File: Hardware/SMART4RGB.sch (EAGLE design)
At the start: 14 parts, among them IC1 WS2811-SOP8, IC2 WS2811-SOP8, IC3 WS2811-SOP8, IC4 WS2811-SOP8, SW1 QG16F-RGB, SW2 QG16F-RGB, SW3 QG16F-RGB, SW4 QG16F-RGB

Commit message: Alter size of board and hole locations to match updated controller. Switch green and blue connections to make colours match WS2812 profile.
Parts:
- C1, C2, C3, C4: device freetronics-jon:CAP0603 -> SuperHouse-DiscreteSemi:CAP0603
- H1: value M06X22MM -> M02X6-SOCKET; device freetronics-jon:M06X22MM -> SuperHouse-Connectors:M02X6-SOCKET
- IC1, IC2, IC3, IC4: device freetronics-jon:WS2811-SOP8 -> SuperHouse-ICs:WS2811-SOP8
- R1: device freetronics-jon:RESISTOR0603 -> SuperHouse-DiscreteSemi:RESISTOR0603
- SW1, SW2, SW3, SW4: device freetronics-jon:QG16F-RGB -> SuperHouse-Switches:QG16F-RGB
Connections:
- net LED1B: now also SW1.G; no longer SW1.B
- net LED1G: now also SW1.B; no longer SW1.G
- net LED2B: now also SW2.G; no longer SW2.B
- net LED2G: now also SW2.B; no longer SW2.G
- net LED3B: now also SW3.G; no longer SW3.B
- net LED3G: now also SW3.B; no longer SW3.G
- net LED4B: now also SW4.G; no longer SW4.B
- net LED4G: now also SW4.B; no longer SW4.G
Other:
- note added: "(C)2018-2020 SuperHouse Automation Pty Ltd: www.superhouse.tv"
- note added: "Green / blue outputs are reversed on WS2811 when controlled using the WS2812 drivers. LED lines switched to make the output match colour commands."
- note added: "V2.0 (2020-11-06)"
- note removed: "(C)2018 SuperHouse Automation Pty Ltd: www.superhouse.tv"
- note removed: "V1.0 (2018-04-11)"

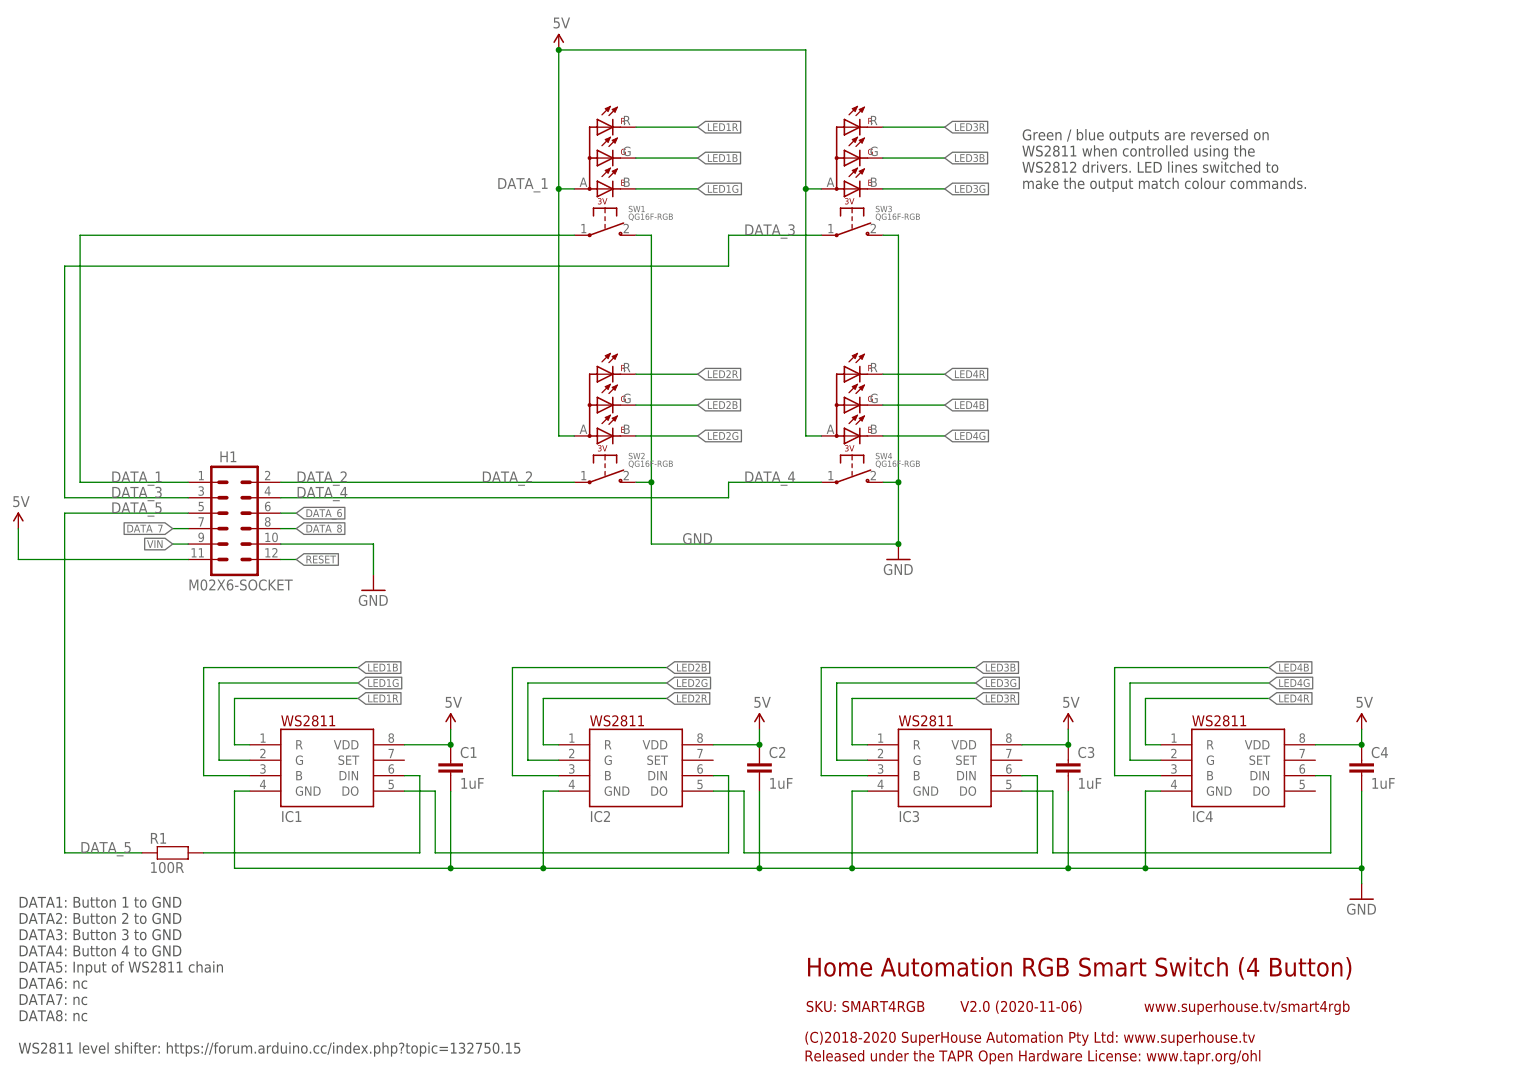
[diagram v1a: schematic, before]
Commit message: Converted switch isolation from FETs to diodes for v2.1 release.
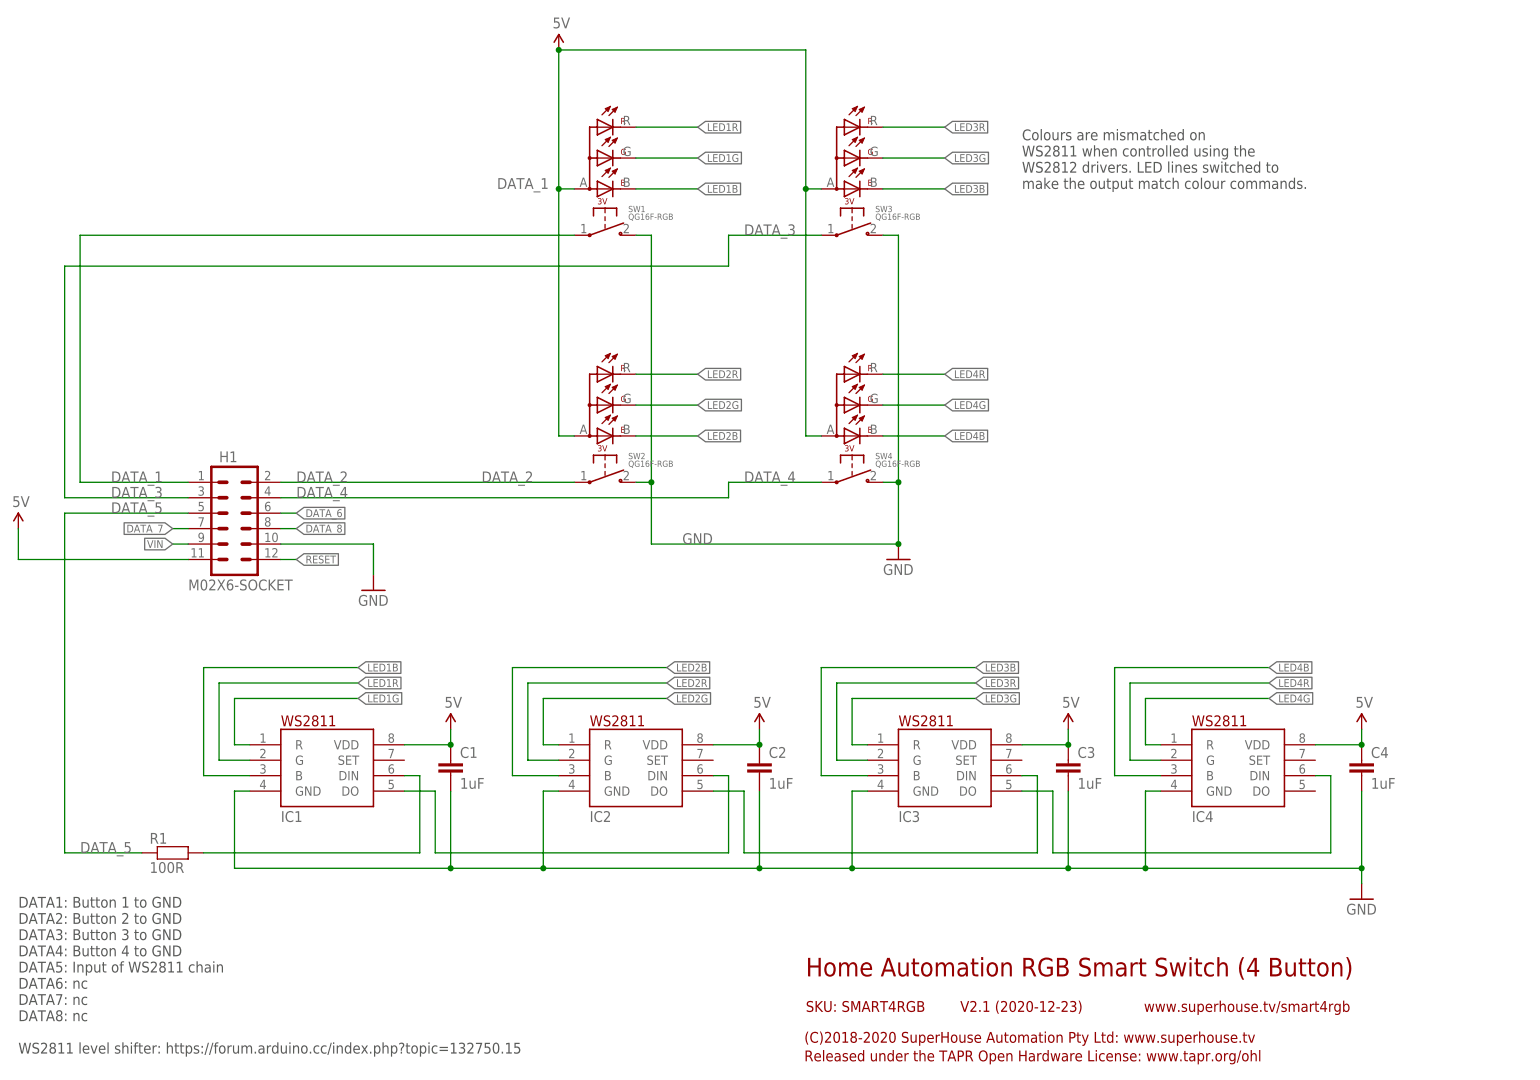
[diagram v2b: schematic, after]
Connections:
- net LED1B: now also SW1.B; no longer SW1.G
- net LED1G: now also IC1.R, SW1.G; no longer IC1.G, SW1.B
- net LED1R: now also IC1.G; no longer IC1.R
- net LED2B: now also SW2.B; no longer SW2.G
- net LED2G: now also IC2.R, SW2.G; no longer IC2.G, SW2.B
- net LED2R: now also IC2.G; no longer IC2.R
- net LED3B: now also SW3.B; no longer SW3.G
- net LED3G: now also IC3.R, SW3.G; no longer IC3.G, SW3.B
- net LED3R: now also IC3.G; no longer IC3.R
- net LED4B: now also SW4.B; no longer SW4.G
- net LED4G: now also IC4.R, SW4.G; no longer IC4.G, SW4.B
- net LED4R: now also IC4.G; no longer IC4.R
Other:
- note added: "Colours are mismatched on WS2811 when controlled using the WS2812 drivers. LED lines switched to make the output match colour commands."
- note added: "V2.1 (2020-12-23)"
- note removed: "Green / blue outputs are reversed on WS2811 when controlled using the WS2812 drivers. LED lines switched to make the output match colour commands."
- note removed: "V2.0 (2020-11-06)"
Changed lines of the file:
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@@
 <frame x1="0" y1="0" x2="248.92" y2="185.42" columns="8" rows="5" layer="94"/>
 <text x="139.7" y="20.32" size="3.048" layer="94">Home Automation RGB Smart Switch (4 Button)</text>
-<text x="165.1" y="14.478" size="1.778" layer="94">V2.0 (2020-11-06)</text>
+<text x="165.1" y="14.478" size="1.778" layer="94">V2.1 (2020-12-23)</text>
 <text x="139.7" y="14.478" size="1.778" layer="94">SKU: SMART4RGB</text>
 <text x="139.446" y="9.398" size="1.778" layer="94">(C)2018-2020 SuperHouse Automation Pty Ltd: www.superhouse.tv</text>
@@
 DATA8: nc
 WS2811 level shifter: https://forum.arduino.cc/index.php?topic=132750.15</text>
-<text x="175.26" y="149.86" size="1.778" layer="97">Green / blue outputs are reversed on
+<text x="175.26" y="149.86" size="1.778" layer="97">Colours are mismatched on
 WS2811 when controlled using the
 WS2812 drivers. LED lines switched to
@@
 </segment>
 <segment>
-<pinref part="SW1" gate="G$1" pin="G"/>
-<wire x1="111.76" y1="154.94" x2="121.92" y2="154.94" width="0.1524" layer="91"/>
-<label x="121.92" y="154.94" size="1.27" layer="95" xref="yes"/>
+<wire x1="111.76" y1="149.86" x2="121.92" y2="149.86" width="0.1524" layer="91"/>
+<pinref part="SW1" gate="G$1" pin="B"/>
+<label x="121.92" y="149.86" size="1.27" layer="95" xref="yes"/>
 </segment>
 </net>
@@
 </segment>
 <segment>
-<pinref part="SW2" gate="G$1" pin="G"/>
-<wire x1="111.76" y1="114.3" x2="121.92" y2="114.3" width="0.1524" layer="91"/>
-<label x="121.92" y="114.3" size="1.27" layer="95" xref="yes"/>
+<wire x1="111.76" y1="109.22" x2="121.92" y2="109.22" width="0.1524" layer="91"/>
+<pinref part="SW2" gate="G$1" pin="B"/>
+<label x="121.92" y="109.22" size="1.27" layer="95" xref="yes"/>
 </segment>
 </net>
@@
 </segment>
 <segment>
-<pinref part="SW3" gate="G$1" pin="G"/>
-<wire x1="152.4" y1="154.94" x2="162.56" y2="154.94" width="0.1524" layer="91"/>
-<label x="162.56" y="154.94" size="1.27" layer="95" xref="yes"/>
+<wire x1="152.4" y1="149.86" x2="162.56" y2="149.86" width="0.1524" layer="91"/>
+<pinref part="SW3" gate="G$1" pin="B"/>
+<label x="162.56" y="149.86" size="1.27" layer="95" xref="yes"/>
 </segment>
 </net>
@@
 </segment>
 <segment>
-<pinref part="SW4" gate="G$1" pin="G"/>
-<wire x1="152.4" y1="114.3" x2="162.56" y2="114.3" width="0.1524" layer="91"/>
-<label x="162.56" y="114.3" size="1.27" layer="95" xref="yes"/>
+<wire x1="152.4" y1="109.22" x2="162.56" y2="109.22" width="0.1524" layer="91"/>
+<pinref part="SW4" gate="G$1" pin="B"/>
+<label x="162.56" y="109.22" size="1.27" layer="95" xref="yes"/>
 </segment>
 </net>
@@
 </segment>
 <segment>
+<pinref part="IC1" gate="G$1" pin="G"/>
+<wire x1="48.26" y1="55.88" x2="43.18" y2="55.88" width="0.1524" layer="91"/>
+<wire x1="43.18" y1="55.88" x2="43.18" y2="68.58" width="0.1524" layer="91"/>
+<wire x1="43.18" y1="68.58" x2="66.04" y2="68.58" width="0.1524" layer="91"/>
+<label x="66.04" y="68.58" size="1.27" layer="95" xref="yes"/>
+</segment>
+</net>
+<net name="LED1G" class="0">
+<segment>
+<pinref part="SW1" gate="G$1" pin="G"/>
+<wire x1="111.76" y1="154.94" x2="121.92" y2="154.94" width="0.1524" layer="91"/>
+<label x="121.92" y="154.94" size="1.27" layer="95" xref="yes"/>
+</segment>
+<segment>
 <pinref part="IC1" gate="G$1" pin="R"/>
 <wire x1="48.26" y1="58.42" x2="45.72" y2="58.42" width="0.1524" layer="91"/>
@@
 </segment>
 </net>
-<net name="LED1G" class="0">
-<segment>
-<pinref part="IC1" gate="G$1" pin="G"/>
-<wire x1="48.26" y1="55.88" x2="43.18" y2="55.88" width="0.1524" layer="91"/>
-<wire x1="43.18" y1="55.88" x2="43.18" y2="68.58" width="0.1524" layer="91"/>
-<wire x1="43.18" y1="68.58" x2="66.04" y2="68.58" width="0.1524" layer="91"/>
-<label x="66.04" y="68.58" size="1.27" layer="95" xref="yes"/>
-</segment>
-<segment>
-<wire x1="111.76" y1="149.86" x2="121.92" y2="149.86" width="0.1524" layer="91"/>
-<pinref part="SW1" gate="G$1" pin="B"/>
-<label x="121.92" y="149.86" size="1.27" layer="95" xref="yes"/>
-</segment>
-</net>
 <net name="LED3G" class="0">
+<segment>
+<pinref part="SW3" gate="G$1" pin="G"/>
+<wire x1="152.4" y1="154.94" x2="162.56" y2="154.94" width="0.1524" layer="91"/>
+<label x="162.56" y="154.94" size="1.27" layer="95" xref="yes"/>
+</segment>
+<segment>
+<pinref part="IC3" gate="G$1" pin="R"/>
+<wire x1="149.86" y1="58.42" x2="147.32" y2="58.42" width="0.1524" layer="91"/>
+<wire x1="147.32" y1="58.42" x2="147.32" y2="66.04" width="0.1524" layer="91"/>
+<wire x1="147.32" y1="66.04" x2="167.64" y2="66.04" width="0.1524" layer="91"/>
+<label x="167.64" y="66.04" size="1.27" layer="95" xref="yes"/>
+</segment>
+</net>
+<net name="LED3R" class="0">
+<segment>
+<pinref part="SW3" gate="G$1" pin="R"/>
+<wire x1="152.4" y1="160.02" x2="162.56" y2="160.02" width="0.1524" layer="91"/>
+<label x="162.56" y="160.02" size="1.27" layer="95" xref="yes"/>
+</segment>
 <segment>
 <pinref part="IC3" gate="G$1" pin="G"/>
@@
 <label x="167.64" y="68.58" size="1.27" layer="95" xref="yes"/>
 </segment>
-<segment>
-<wire x1="152.4" y1="149.86" x2="162.56" y2="149.86" width="0.1524" layer="91"/>
-<pinref part="SW3" gate="G$1" pin="B"/>
-<label x="162.56" y="149.86" size="1.27" layer="95" xref="yes"/>
-</segment>
-</net>
-<net name="LED3R" class="0">
-<segment>
-<pinref part="SW3" gate="G$1" pin="R"/>
-<wire x1="152.4" y1="160.02" x2="162.56" y2="160.02" width="0.1524" layer="91"/>
-<label x="162.56" y="160.02" size="1.27" layer="95" xref="yes"/>
-</segment>
-<segment>
-<pinref part="IC3" gate="G$1" pin="R"/>
-<wire x1="149.86" y1="58.42" x2="147.32" y2="58.42" width="0.1524" layer="91"/>
-<wire x1="147.32" y1="58.42" x2="147.32" y2="66.04" width="0.1524" layer="91"/>
-<wire x1="147.32" y1="66.04" x2="167.64" y2="66.04" width="0.1524" layer="91"/>
-<label x="167.64" y="66.04" size="1.27" layer="95" xref="yes"/>
-</segment>
 </net>
 <net name="LED2G" class="0">
+<segment>
+<pinref part="SW2" gate="G$1" pin="G"/>
+<wire x1="111.76" y1="114.3" x2="121.92" y2="114.3" width="0.1524" layer="91"/>
+<label x="121.92" y="114.3" size="1.27" layer="95" xref="yes"/>
+</segment>
+<segment>
+<pinref part="IC2" gate="G$1" pin="R"/>
+<wire x1="99.06" y1="58.42" x2="96.52" y2="58.42" width="0.1524" layer="91"/>
+<wire x1="96.52" y1="58.42" x2="96.52" y2="66.04" width="0.1524" layer="91"/>
+<wire x1="96.52" y1="66.04" x2="116.84" y2="66.04" width="0.1524" layer="91"/>
+<label x="116.84" y="66.04" size="1.27" layer="95" xref="yes"/>
+</segment>
+</net>
+<net name="LED2R" class="0">
+<segment>
+<pinref part="SW2" gate="G$1" pin="R"/>
+<wire x1="111.76" y1="119.38" x2="121.92" y2="119.38" width="0.1524" layer="91"/>
+<label x="121.92" y="119.38" size="1.27" layer="95" xref="yes"/>
+</segment>
 <segment>
 <pinref part="IC2" gate="G$1" pin="G"/>
@@
 <label x="116.84" y="68.58" size="1.27" layer="95" xref="yes"/>
 </segment>
-<segment>
-<wire x1="111.76" y1="109.22" x2="121.92" y2="109.22" width="0.1524" layer="91"/>
-<pinref part="SW2" gate="G$1" pin="B"/>
-<label x="121.92" y="109.22" size="1.27" layer="95" xref="yes"/>
-</segment>
-</net>
-<net name="LED2R" class="0">
-<segment>
-<pinref part="SW2" gate="G$1" pin="R"/>
-<wire x1="111.76" y1="119.38" x2="121.92" y2="119.38" width="0.1524" layer="91"/>
-<label x="121.92" y="119.38" size="1.27" layer="95" xref="yes"/>
-</segment>
-<segment>
-<pinref part="IC2" gate="G$1" pin="R"/>
-<wire x1="99.06" y1="58.42" x2="96.52" y2="58.42" width="0.1524" layer="91"/>
-<wire x1="96.52" y1="58.42" x2="96.52" y2="66.04" width="0.1524" layer="91"/>
-<wire x1="96.52" y1="66.04" x2="116.84" y2="66.04" width="0.1524" layer="91"/>
-<label x="116.84" y="66.04" size="1.27" layer="95" xref="yes"/>
-</segment>
 </net>
 <net name="LED4G" class="0">
+<segment>
+<pinref part="SW4" gate="G$1" pin="G"/>
+<wire x1="152.4" y1="114.3" x2="162.56" y2="114.3" width="0.1524" layer="91"/>
+<label x="162.56" y="114.3" size="1.27" layer="95" xref="yes"/>
+</segment>
+<segment>
+<pinref part="IC4" gate="G$1" pin="R"/>
+<wire x1="198.12" y1="58.42" x2="195.58" y2="58.42" width="0.1524" layer="91"/>
+<wire x1="195.58" y1="58.42" x2="195.58" y2="66.04" width="0.1524" layer="91"/>
+<wire x1="195.58" y1="66.04" x2="215.9" y2="66.04" width="0.1524" layer="91"/>
+<label x="215.9" y="66.04" size="1.27" layer="95" xref="yes"/>
+</segment>
+</net>
+<net name="LED4R" class="0">
+<segment>
+<pinref part="SW4" gate="G$1" pin="R"/>
+<wire x1="152.4" y1="119.38" x2="162.56" y2="119.38" width="0.1524" layer="91"/>
+<label x="162.56" y="119.38" size="1.27" layer="95" xref="yes"/>
+</segment>
 <segment>
 <pinref part="IC4" gate="G$1" pin="G"/>
@@
 <label x="215.9" y="68.58" size="1.27" layer="95" xref="yes"/>
 </segment>
-<segment>
-<wire x1="152.4" y1="109.22" x2="162.56" y2="109.22" width="0.1524" layer="91"/>
-<pinref part="SW4" gate="G$1" pin="B"/>
-<label x="162.56" y="109.22" size="1.27" layer="95" xref="yes"/>
-</segment>
-</net>
-<net name="LED4R" class="0">
-<segment>
-<pinref part="SW4" gate="G$1" pin="R"/>
-<wire x1="152.4" y1="119.38" x2="162.56" y2="119.38" width="0.1524" layer="91"/>
-<label x="162.56" y="119.38" size="1.27" layer="95" xref="yes"/>
-</segment>
-<segment>
-<pinref part="IC4" gate="G$1" pin="R"/>
-<wire x1="198.12" y1="58.42" x2="195.58" y2="58.42" width="0.1524" layer="91"/>
-<wire x1="195.58" y1="58.42" x2="195.58" y2="66.04" width="0.1524" layer="91"/>
-<wire x1="195.58" y1="66.04" x2="215.9" y2="66.04" width="0.1524" layer="91"/>
-<label x="215.9" y="66.04" size="1.27" layer="95" xref="yes"/>
-</segment>
-</net>
+</net>
